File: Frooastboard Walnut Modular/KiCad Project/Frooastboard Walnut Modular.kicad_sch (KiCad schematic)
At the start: 68 parts, among them J1 SW Interface, J2 Conn_02x10_Odd_Even, U1 RP2040, U2 SPX3819M5-L-3-3, U3 W25Q32JVZP, U4 nRF8001, U5 TP4056, U6 FS312F-G, U7 FS8205, Y1 32.768kHz, Y2 16MHz, Y3 12MHz

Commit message: Switch to IP2312
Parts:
- removed C28: 10u, Capacitor_SMD:C_0805_2012Metric, symbol Device:C_Small
- removed R11: 1k2, Resistor_SMD:R_0805_2012Metric, symbol Device:R_Small
- removed U5: TP4056, Package_SO:SOIC-8-1EP_3.9x4.9mm_P1.27mm_EP2.41x3.3mm, symbol Frooastboard Symbols:TP4056
- added C?: 22u, symbol Device:C
- added C? (x2): 10u, symbol Device:C
- added L?: 1uH, symbol Device:L
- added R? (x2): 0k1, symbol Device:R
- added R?: 2R, symbol Device:R
- added R?: 1k, Resistor_SMD:R_0805_2012Metric, symbol Device:R_Small
- added R?: 51k, symbol Device:R
- added U?: IP2312, Package_SO:SOIC-8-1EP_3.9x4.9mm_P1.27mm_EP2.41x3.3mm, symbol Frooastboard Symbols:IP2312
- C30: value 100n -> 22u
- R12: value 100R -> 0k5
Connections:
- net BATT+ is gone; now on net BATTERY+: R12.1, R13.1, TP6.2, U2.1 (IN), U2.3 (EN)
- net +5V: now also C?.1, C?.1, R?.1, U?.8 (VIN)
- net GND: now also C?.2, C?.2, C?.2, R?.1, U?.9 (EP)
- net BATTERY+: now reaches C30.1, U6.5 (VCC)
- net BATTERY+: now also L?.2, R?.1; no longer R12.2
- net BATT-: now reaches C30.2, TP6.1, U6.6 (GND), U7.3 (S2)
- new net: R?.2, U?.1 (D1)
- new net: R12.2, U?.5 (BAT)
- new net: C?.1, R?.2
- new net: R?.2, U?.2 (TEST)
- new net: R?.2, U?.3 (D2)
- new net: L?.1, U?.7 (SW)
- new net: R?.2, U?.4 (NTC)
- new net LED_CHARGING: R?.1
- new net LED_FULL: R?.1
- no-connect marks 5 -> 9
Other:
- note added: "NC for 2.1A"
- note added: "NC for 4.2V"
- moved on the sheet: C14, C15, C16, C17, C18, C19, C20, C21, C22, C23, C24, C25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

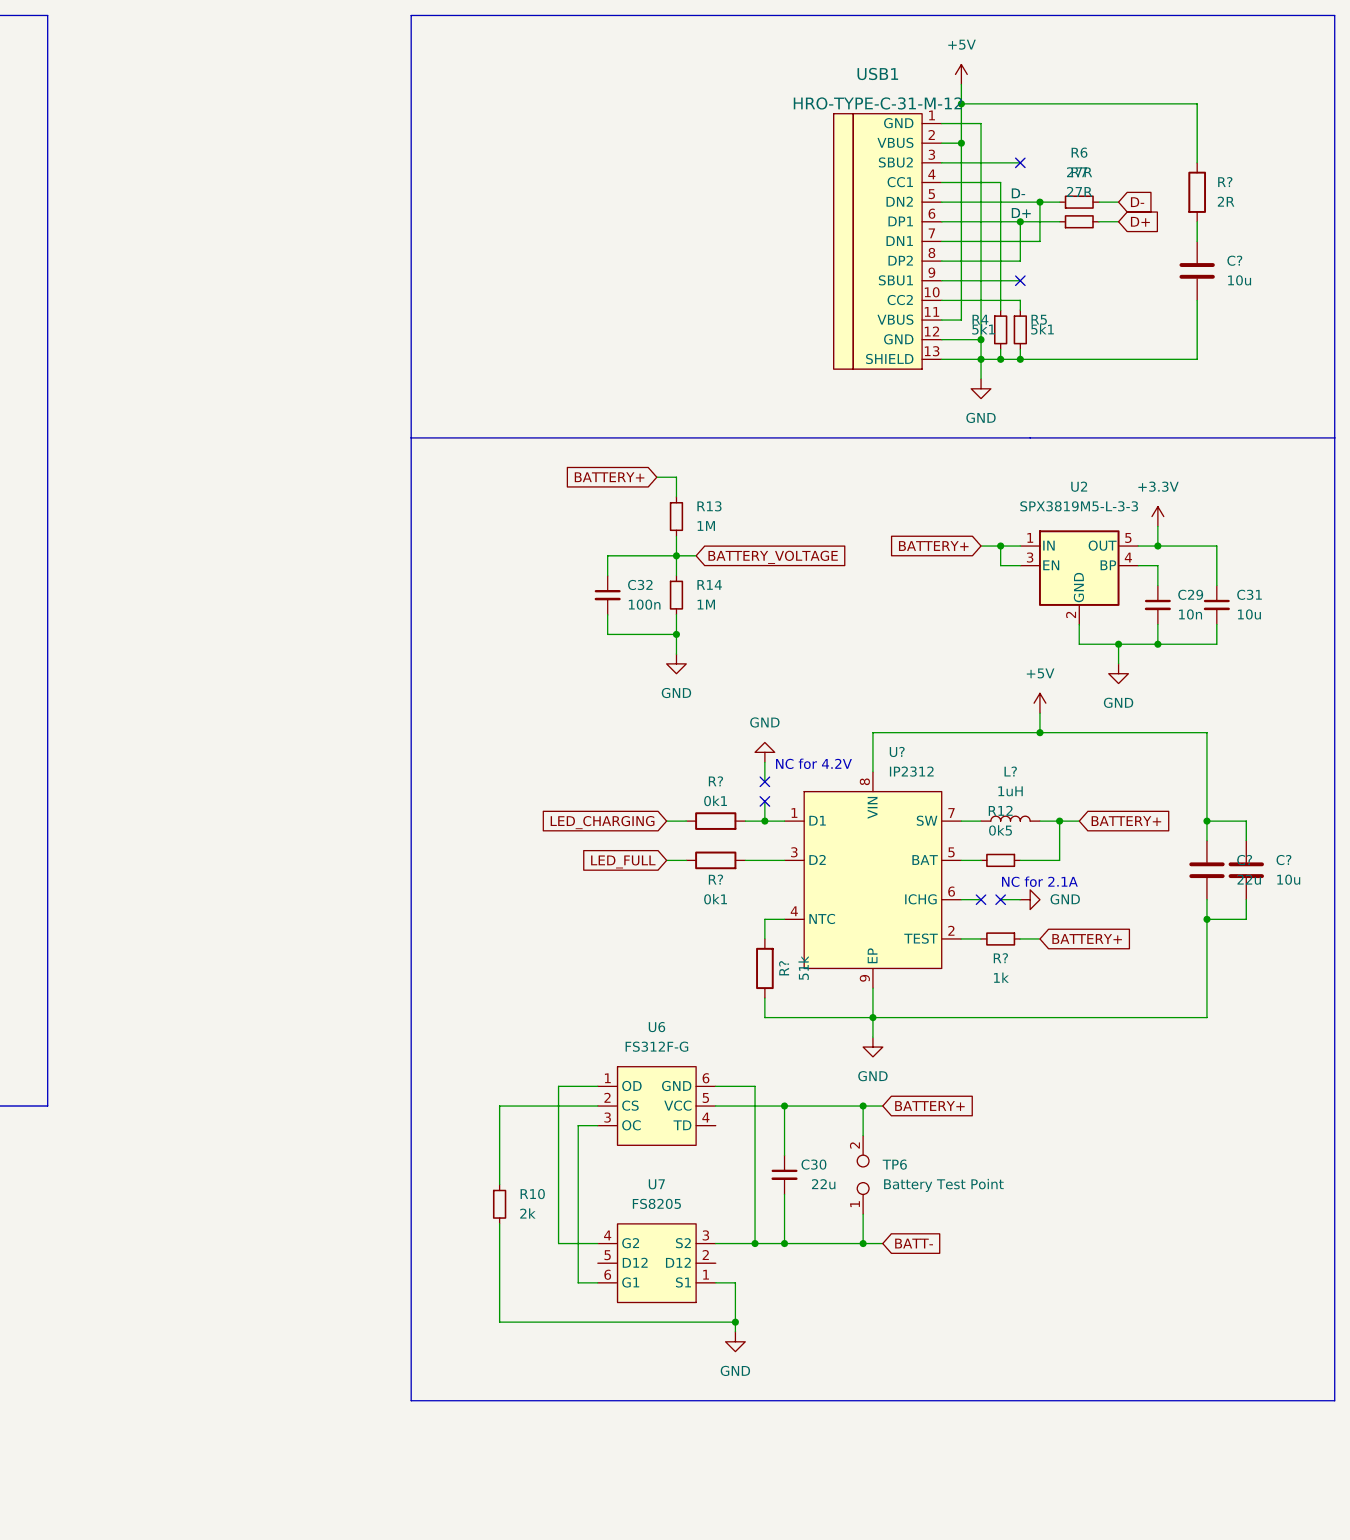
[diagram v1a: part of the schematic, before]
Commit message: Update Frooastboard Walnut Modular.kicad_sch
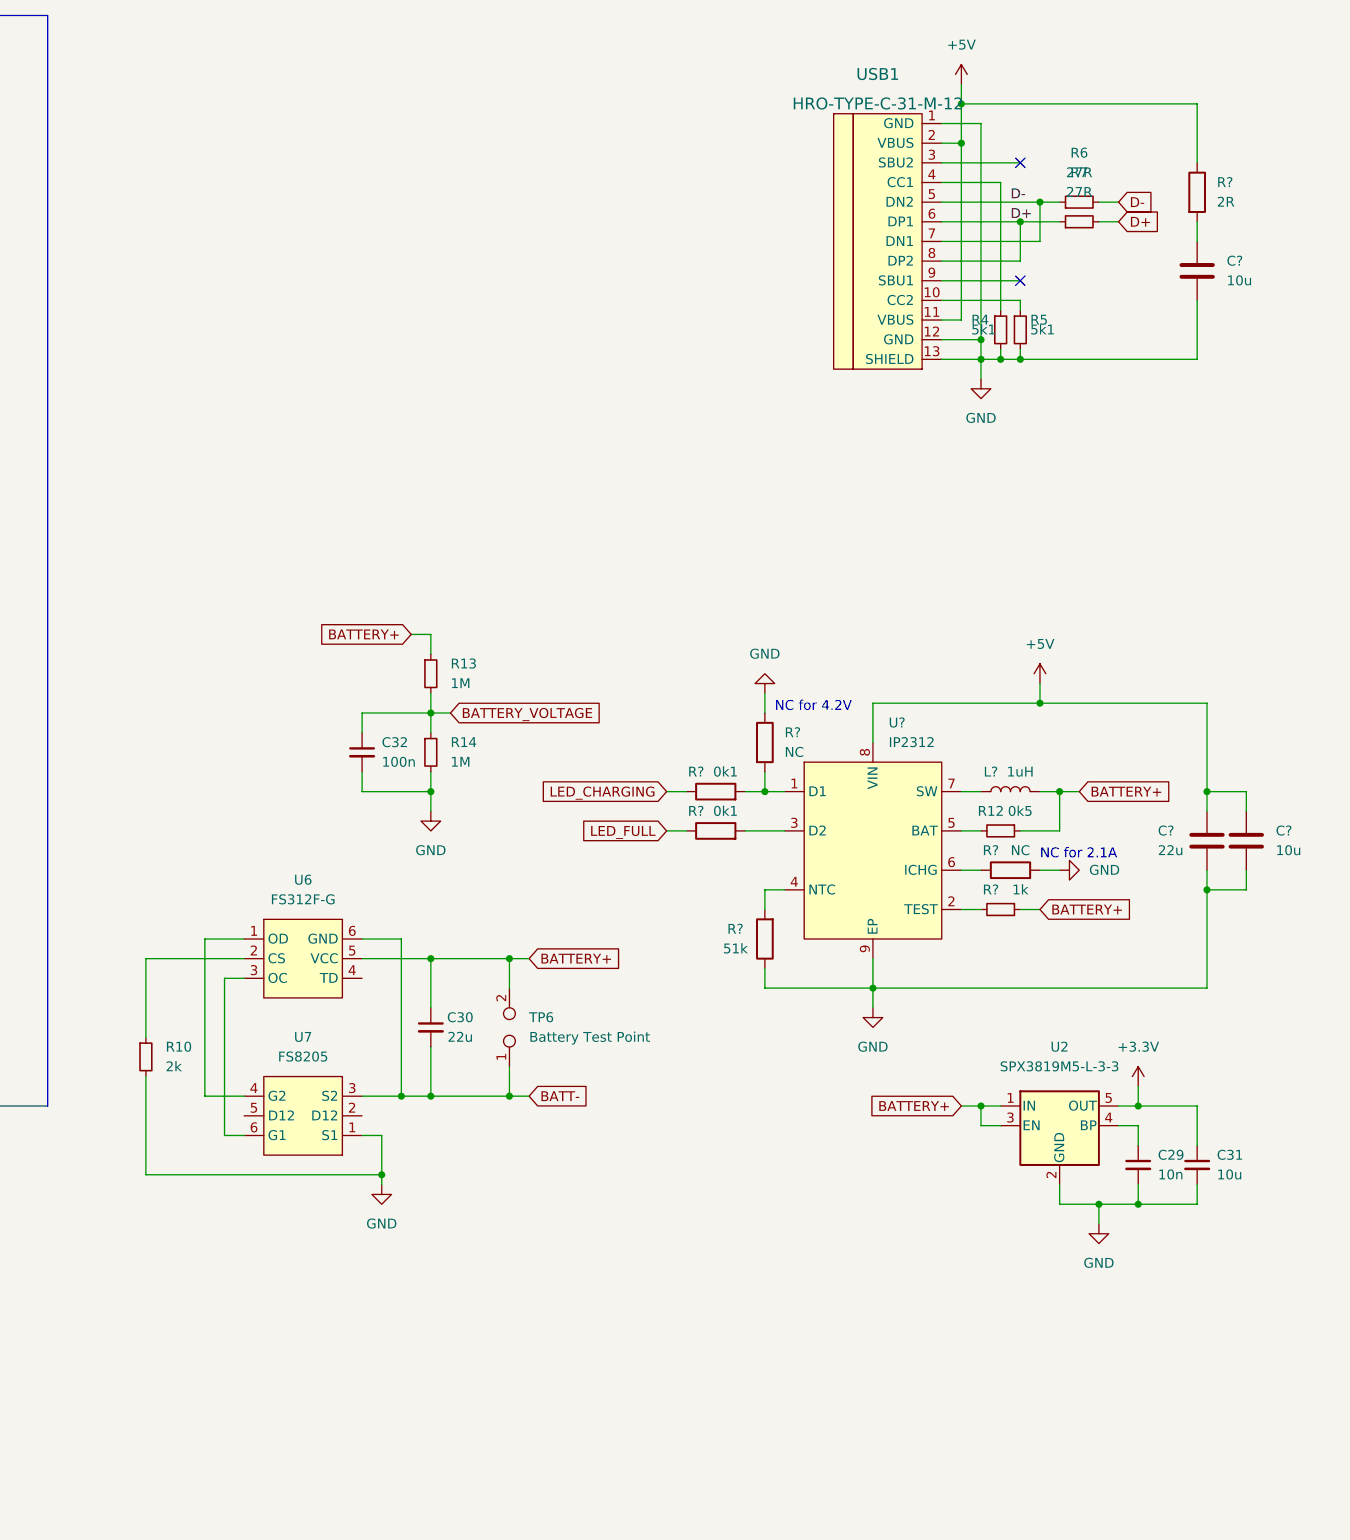
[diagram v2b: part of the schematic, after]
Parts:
- added R? (x2): NC, symbol Device:R
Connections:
- net GND: now also R?.1, R?.2
- net at R?.2, U?.1 (D1): now also R?.2
- net at U?.6 (ICHG): now also R?.1
- no-connect marks 9 -> 5
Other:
- moved on the sheet: C29, C30, C31, C32, C?, L?, R10, R12, R13, R14, R?, TP6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

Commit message: do some stuff
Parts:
- removed C?: 10u, symbol Device:C
- removed J2: Conn_02x10_Odd_Even, symbol Connector_Generic:Conn_02x10_Odd_Even
- removed R4, R5: 5k1, Resistor_SMD:R_0805_2012Metric, symbol Device:R_Small
- removed R6, R7: 27R, Resistor_SMD:R_0805_2012Metric, symbol Device:R_Small
- removed R?: 2R, symbol Device:R
- removed USB1: HRO-TYPE-C-31-M-12, Type_C:HRO-TYPE-C-31-M-12, symbol Type-C:HRO-TYPE-C-31-M-12
- added C28: 0.1u, Capacitor_SMD:C_0805_2012Metric, symbol Device:C_Small
- added C33: 10u, Capacitor_SMD:C_0805_2012Metric, symbol Device:C_Small
- added C34, C35: 10u, Capacitor_Tantalum_SMD:CP_EIA-2012-15_AVX-P, symbol Device:C_Polarized
- added D1: GREEN, symbol Device:LED
- added D10, D100, D101, D102, D103, D104, D11, D12, D13, D14, D17, D18, D19, D20, D24, D25, D26, D27, D3, D30, D31, D32, D33, D37, D38, D39, D4, D40, D43, D44, D45, D46, D49, D5, D50, D51, D52, D55, D56, D57, D58, D59, D6, D60, D61, D62, D7, D74, D75, D76, D77, D8, D89, D9, D90, D91, D92, D93, D94, D95, D96, D97, D98, D99: RGB_LED_6_Pin, Frooastboard Footprints:Everlight 99-235, symbol Frooastboard Symbols:RGB_LED_6_Pin
- added D15, D16, D21, D22, D23, D28, D29, D34, D35, D36, D41, D42, D47, D48, D53, D54, D63, D64, D65, D66, D67, D68, D69, D70, D71, D72, D73, D78, D79, D80, D81, D82, D83, D84, D85, D86, D87, D88: D_Small, symbol Device:D_Small
- added D2: RED, symbol Device:LED
- added J10: Conn_01x13_Male, symbol Connector:Conn_01x13_Male
- added J11: Conn_01x13_Female, symbol Connector:Conn_01x13_Female
- added J2: Conn_01x16, symbol Connector_Generic:Conn_01x16
- added J3, J4: Conn_01x06, symbol Connector_Generic:Conn_01x06
- added J5: Conn_01x10, symbol Connector_Generic:Conn_01x10
- added J6: Conn_01x12, symbol Connector_Generic:Conn_01x12
- added J7: Conn_01x04, symbol Connector_Generic:Conn_01x04
- added J8: Conn_01x10_Male, symbol Connector:Conn_01x10_Male
- added J9: Conn_01x10_Female, symbol Connector:Conn_01x10_Female
- added M1: Frooastboard_MM2040, symbol Frooastboard Symbols:Frooastboard_MM2040
- added MX1, MX10, MX11, MX12, MX13, MX14, MX15, MX16, MX17, MX18, MX19, MX2, MX20, MX21, MX22, MX23, MX24, MX25, MX26, MX27, MX28, MX29, MX3, MX30, MX31, MX32, MX33, MX34, MX35, MX36, MX37, MX38, MX4, MX5, MX6, MX7, MX8, MX9: MX-NoLED, symbol MX_Alps_Hybrid:MX-NoLED
- added R11, R7: 100k, Resistor_SMD:R_0805_2012Metric, symbol Device:R
- added R4, R5: 2k, Resistor_SMD:R_0805_2012Metric, symbol Device:R
- added R6: 20k, Resistor_SMD:R_0805_2012Metric, symbol Device:R
- added U5: IS31FL3733-QF, Package_DFN_QFN:QFN-48-1EP_6x6mm_P0.4mm_EP4.2x4.2mm, symbol Driver_LED:IS31FL3733-QF
- U1: footprint Frooastboard Footprints:RP2040-QFN-56 -> Sleep-Lib:RP2040-QFN-56
- gave numbers to parts that had none: 10
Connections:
- net +3V3: now also C28.2, C33.1, C34.1, C35.1, R11.2, R4.1, R5.1, U5.20 (PVCC), U5.29 (PVCC), U5.37 (AVCC), U5.38 (DVCC), U5.39 (VIO)
- net +5V: now also J7.1 (Pin_1)
- net COL0: now also J5.1 (Pin_1), J9.1 (Pin_1)
- net COL1: now also J5.2 (Pin_2), J9.2 (Pin_2)
- net COL2: now also J5.3 (Pin_3), J9.3 (Pin_3)
- net COL3: now also J5.4 (Pin_4), J9.4 (Pin_4)
- net COL4: now also J5.5 (Pin_5), J9.5 (Pin_5)
- net COL5: now also J5.6 (Pin_6), J9.6 (Pin_6)
- net COL6: now also J5.7 (Pin_7), J9.7 (Pin_7)
- net COL7: now also J5.8 (Pin_8), J9.8 (Pin_8)
- net COL8: now also J11.1 (Pin_1), J5.9 (Pin_9)
- net COL9: now also J11.2 (Pin_2), J5.10 (Pin_10)
- net GND: now also C28.1, C33.2, C34.2, C35.2, D1.1 (K), D2.1 (K), J7.2 (Pin_2), R6.2, R7.2, U5.12 (PGND), U5.34 (AGND), U5.43 (ADDR1), U5.44 (ADDR2), U5.48 (GND), U5.49 (GND), U5.5 (PGND)
- net LED_CHARGING: now also D2.2 (A)
- net LED_FULL: now also D1.2 (A)
- net ROW0: now also J11.3 (Pin_3), J6.1 (Pin_1)
- net ROW1: now also J11.4 (Pin_4), J6.2 (Pin_2)
- net ROW2: now also J11.5 (Pin_5), J6.3 (Pin_3)
- net ROW3: now also J11.6 (Pin_6), J6.4 (Pin_4)
- net ROW4: now also J11.7 (Pin_7), J6.5 (Pin_5)
- net ROW5: now also J11.8 (Pin_8), J6.6 (Pin_6)
- net ROW6: now also J11.9 (Pin_9), J6.7 (Pin_7)
- net ROW7: now also J11.10 (Pin_10), J6.8 (Pin_8)
- net ROW8: now also J11.11 (Pin_11), J6.9 (Pin_9)
- net ROW9: now also J11.12 (Pin_12), J6.10 (Pin_10), J9.9 (Pin_9)
- net SCL: now also R5.2, U5.42 (SCL)
- net SDA: now also R4.2, U5.41 (SDA)
- net ROW10: now reaches U1.37 (GPIO25)
- net ROW10: now also J11.13 (Pin_13), J6.11 (Pin_11), J9.10 (Pin_10)
- net D+ renamed RP_D+
- net RP_D+: now also J7.3 (Pin_3)
- net D- renamed RP_D-
- net RP_D-: now also J7.4 (Pin_4)
- new net: J8.3 (Pin_3), MX5.1 (COL), MX6.1 (COL)
- new net: D23.2 (A), MX5.2 (ROW)
- new net: D16.1 (K), D22.1 (K), D28.1 (K), D34.1 (K), D36.1 (K), D42.1 (K), D48.1 (K), D54.1 (K), J8.10 (Pin_10)
- new net: D48.2 (A), MX14.2 (ROW)
- new net: J8.1 (Pin_1), MX1.1 (COL), MX2.1 (COL)
- new net: J8.2 (Pin_2), MX3.1 (COL), MX4.1 (COL)
- new net: J8.4 (Pin_4), MX7.1 (COL), MX8.1 (COL)
- new net: J8.5 (Pin_5), MX10.1 (COL), MX9.1 (COL)
- new net: J8.6 (Pin_6), MX11.1 (COL), MX12.1 (COL)
- new net: J8.7 (Pin_7), MX13.1 (COL), MX14.1 (COL)
- new net: J8.8 (Pin_8), MX15.1 (COL), MX16.1 (COL)
- new net: D15.1 (K), D21.1 (K), D23.1 (K), D29.1 (K), D35.1 (K), D41.1 (K), D47.1 (K), D53.1 (K), J8.9 (Pin_9)
- new net: J10.1 (Pin_1), MX17.1 (COL), MX18.1 (COL), MX19.1 (COL), MX20.1 (COL), MX21.1 (COL), MX22.1 (COL), MX23.1 (COL), MX24.1 (COL), MX25.1 (COL), MX26.1 (COL), MX27.1 (COL)
- new net: D71.2 (A), MX25.2 (ROW)
- new net: D36.2 (A), MX10.2 (ROW)
- new net: D73.1 (K), D88.1 (K), J10.12 (Pin_12)
- new net: D73.2 (A), MX27.2 (ROW)
- new net: D16.2 (A), MX2.2 (ROW)
- new net: D47.2 (A), MX13.2 (ROW)
- new net: D88.2 (A), MX38.2 (ROW)
- new net: J10.2 (Pin_2), MX28.1 (COL), MX29.1 (COL), MX30.1 (COL), MX31.1 (COL), MX32.1 (COL), MX33.1 (COL), MX34.1 (COL), MX35.1 (COL), MX36.1 (COL), MX37.1 (COL), MX38.1 (COL)
- new net: D82.2 (A), MX32.2 (ROW)
- new net: D41.2 (A), MX11.2 (ROW)
- new net: D80.2 (A), MX30.2 (ROW)
- new net: D64.2 (A), MX18.2 (ROW)
- new net: D70.2 (A), MX24.2 (ROW)
- new net: D15.2 (A), MX1.2 (ROW)
- new net: D66.2 (A), MX20.2 (ROW)
- new net: D63.1 (K), D78.1 (K), J10.3 (Pin_3)
- new net: D78.2 (A), MX28.2 (ROW)
- new net: D22.2 (A), MX4.2 (ROW)
- new net: D72.1 (K), D87.1 (K), J10.10 (Pin_10)
- new net: D67.1 (K), D82.1 (K), J10.11 (Pin_11)
- new net: D68.1 (K), D83.1 (K), J10.13 (Pin_13)
- new net: D69.1 (K), D84.1 (K), J10.4 (Pin_4)
- new net: D64.1 (K), D79.1 (K), J10.5 (Pin_5)
- new net: D70.1 (K), D85.1 (K), J10.6 (Pin_6)
- new net: D65.1 (K), D80.1 (K), J10.7 (Pin_7)
- new net: D71.1 (K), D86.1 (K), J10.8 (Pin_8)
- new net: D66.1 (K), D81.1 (K), J10.9 (Pin_9)
- new net: D21.2 (A), MX3.2 (ROW)
- new net: D81.2 (A), MX31.2 (ROW)
- new net: D42.2 (A), MX12.2 (ROW)
- new net: D83.2 (A), MX33.2 (ROW)
- new net: D29.2 (A), MX7.2 (ROW)
- new net: D84.2 (A), MX34.2 (ROW)
- new net: D35.2 (A), MX9.2 (ROW)
- new net: D86.2 (A), MX36.2 (ROW)
- new net: D67.2 (A), MX21.2 (ROW)
- new net: D69.2 (A), MX23.2 (ROW)
- new net: D53.2 (A), MX15.2 (ROW)
- new net: D28.2 (A), MX6.2 (ROW)
- new net: D79.2 (A), MX29.2 (ROW)
- new net: D85.2 (A), MX35.2 (ROW)
- new net: D68.2 (A), MX22.2 (ROW)
- new net: D87.2 (A), MX37.2 (ROW)
- new net: D72.2 (A), MX26.2 (ROW)
- new net: D54.2 (A), MX16.2 (ROW)
- new net: D65.2 (A), MX19.2 (ROW)
- new net: D34.2 (A), MX8.2 (ROW)
- new net: D63.2 (A), MX17.2 (ROW)
- new net CS1: J2.1 (Pin_1), U5.16 (CS1)
- new net CS10: J2.10 (Pin_10), U5.26 (CS10)
- new net CS11: J2.11 (Pin_11), U5.27 (CS11)
- new net CS12: J2.12 (Pin_12), U5.28 (CS12)
- new net CS13: J2.13 (Pin_13), U5.30 (CS13)
- new net CS14: J2.14 (Pin_14), U5.31 (CS14)
- new net CS15: J2.15 (Pin_15), U5.32 (CS15)
- new net CS16: J2.16 (Pin_16), U5.33 (CS16)
- new net CS2: J2.2 (Pin_2), U5.17 (CS2)
- new net CS3: J2.3 (Pin_3), U5.18 (CS3)
- new net CS4: J2.4 (Pin_4), U5.19 (CS4)
- new net CS5: J2.5 (Pin_5), U5.21 (CS5)
- new net CS6: J2.6 (Pin_6), U5.22 (CS6)
- new net CS7: J2.7 (Pin_7), U5.23 (CS7)
- new net CS8: J2.8 (Pin_8), U5.24 (CS8)
- new net CS9: J2.9 (Pin_9), U5.25 (CS9)
- new net IICRST: R7.1, U5.47 (IICRST)
- new net RSET: R6.1, U5.35 (RSET)
- new net SDB: R11.1, U5.46 (~{SDB})
- new net SW1: J3.1 (Pin_1), U5.2 (SW1)
- new net SW10: J4.4 (Pin_4), U5.13 (SW10)
- new net SW11: J4.5 (Pin_5), U5.14 (SW11)
- new net SW12: J4.6 (Pin_6), U5.15 (SW12)
- new net SW2: J3.2 (Pin_2), U5.3 (SW2)
- new net SW3: J3.3 (Pin_3), U5.4 (SW3)
- new net SW4: J3.4 (Pin_4), U5.6 (SW4)
- new net SW5: J3.5 (Pin_5), U5.7 (SW5)
- new net SW6: J3.6 (Pin_6), U5.8 (SW6)
- new net SW7: J4.1 (Pin_1), U5.9 (SW7)
- new net SW8: J4.2 (Pin_2), U5.10 (SW8)
- new net SW9: J4.3 (Pin_3), U5.11 (SW9)
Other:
- added sheet Main (Main.kicad_sch)
- moved on the sheet: C1, C10, C11, C12, C13, C2, C29, C3, C30, C31, C32, C36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

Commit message: almost finish schematic
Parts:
- removed D10, D100, D101, D102, D103, D104, D11, D12, D13, D14, D17, D18, D19, D20, D24, D25, D26, D27, D3, D30, D31, D32, D33, D37, D38, D39, D4, D40, D43, D44, D45, D46, D49, D5, D50, D51, D52, D55, D56, D57, D58, D59, D6, D60, D61, D62, D7, D74, D75, D76, D77, D8, D89, D9, D90, D91, D92, D93, D94, D95, D96, D97, D98, D99: RGB_LED_6_Pin, Frooastboard Footprints:Everlight 99-235, symbol Frooastboard Symbols:RGB_LED_6_Pin
- removed D15, D16, D21, D22, D23, D28, D29, D34, D35, D36, D41, D42, D47, D48, D53, D54, D63, D64, D65, D66, D67, D68, D69, D70, D71, D72, D73, D78, D79, D80, D81, D82, D83, D84, D85, D86, D87, D88: D_Small, symbol Device:D_Small
- removed J10: Conn_01x13_Male, symbol Connector:Conn_01x13_Male
- removed J11: Conn_01x13_Female, symbol Connector:Conn_01x13_Female
- removed J8: Conn_01x10_Male, symbol Connector:Conn_01x10_Male
- removed J9: Conn_01x10_Female, symbol Connector:Conn_01x10_Female
- removed M1: Frooastboard_MM2040, symbol Frooastboard Symbols:Frooastboard_MM2040
- removed MX1, MX10, MX11, MX12, MX13, MX14, MX15, MX16, MX17, MX18, MX19, MX2, MX20, MX21, MX22, MX23, MX24, MX25, MX26, MX27, MX28, MX29, MX3, MX30, MX31, MX32, MX33, MX34, MX35, MX36, MX37, MX38, MX4, MX5, MX6, MX7, MX8, MX9: MX-NoLED, symbol MX_Alps_Hybrid:MX-NoLED
- added R23, R24: 27R, Resistor_SMD:R_0805_2012Metric, symbol Device:R_Small
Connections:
- net RP_D+: now also R23.1; no longer J7.3 (Pin_3)
- net RP_D-: now also R24.1; no longer J7.4 (Pin_4)
- new net: J7.3 (Pin_3), R23.2
- new net: J7.4 (Pin_4), R24.2
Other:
- added sheet F Row (F Row.kicad_sch)
- added sheet Numpad (Numpad.kicad_sch)
- moved on the sheet: C1, C10, C11, C12, C13, C17, C19, C2, C21, C22, C23, C24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

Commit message: before nrf52810
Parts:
- removed C30: 22u, Capacitor_SMD:C_0805_2012Metric, symbol Device:C_Small
- removed R10: 2k, Resistor_SMD:R_0805_2012Metric, symbol Device:R_Small
- removed R12: 0k5, Resistor_SMD:R_0805_2012Metric, symbol Device:R_Small
- removed R19: 1k, Resistor_SMD:R_0805_2012Metric, symbol Device:R_Small
- removed R4, R5: 2k, Resistor_SMD:R_0805_2012Metric, symbol Device:R
- removed TP6: Battery Test Point, symbol Connector:TestPoint_2Pole
- added BT1: Battery_Cell, symbol Device:Battery_Cell
- added C30: 22u, symbol Device:C
- added R10: 2k, symbol Device:R
- added R12: 0k5, symbol Device:R
- added R19: 1k, symbol Device:R
- added R4, R5: 2k, symbol Device:R_Small
- added U?: nRF52810-QCxx, Package_DFN_QFN:QFN-32-1EP_5x5mm_P0.5mm_EP3.6x3.6mm, symbol MCU_Nordic:nRF52810-QCxx
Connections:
- net +3V3: now also R4.2, R5.2
- net GND: now also R10.1
- net NRF_MISO: no longer U1.31 (GPIO20)
- net NRF_MOSI: no longer U1.30 (GPIO19)
- net NRF_SCK: no longer U1.29 (GPIO18)
- net RP_RESET: no longer R8.2, U1.26 (~{RUN})
- net SCL: now also R5.1
- net SDA: now also R4.1
- net at U8.5 (BAT): now also R12.1
- net at U8.2 (TEST): now also R19.1
- net at U6.2 (CS): now also R10.2
- net BATT- renamed -BATT
- net -BATT: now also BT1.2 (-), C30.2
- net BATTERY+ renamed +BATT
- net +BATT: now also BT1.1 (+), C30.1, R12.2, R19.2
- net COL0: no longer names the net of J5.1 (Pin_1), U1.2 (GPIO0)
- net COL1: no longer names the net of J5.2 (Pin_2), U1.3 (GPIO1)
- net COL2: no longer names the net of J5.3 (Pin_3), U1.4 (GPIO2)
- net COL3: no longer names the net of J5.4 (Pin_4), U1.5 (GPIO3)
- net COL4: no longer names the net of J5.5 (Pin_5), U1.6 (GPIO4)
- net COL5: no longer names the net of J5.6 (Pin_6), U1.7 (GPIO5)
- net COL6: no longer names the net of J5.7 (Pin_7), U1.8 (GPIO6)
- net COL7: no longer names the net of J5.8 (Pin_8), U1.9 (GPIO7)
- net COL8: no longer names the net of J5.9 (Pin_9), U1.11 (GPIO8)
- net COL9: no longer names the net of J5.10 (Pin_10), U1.12 (GPIO9)
- net CS1: no longer names the net of J2.1 (Pin_1), U5.16 (CS1)
- net CS10: no longer names the net of J2.10 (Pin_10), U5.26 (CS10)
- net CS11: no longer names the net of J2.11 (Pin_11), U5.27 (CS11)
- net CS12: no longer names the net of J2.12 (Pin_12), U5.28 (CS12)
- net CS13: no longer names the net of J2.13 (Pin_13), U5.30 (CS13)
- net CS14: no longer names the net of J2.14 (Pin_14), U5.31 (CS14)
- net CS15: no longer names the net of J2.15 (Pin_15), U5.32 (CS15)
- net CS16: no longer names the net of J2.16 (Pin_16), U5.33 (CS16)
- net CS2: no longer names the net of J2.2 (Pin_2), U5.17 (CS2)
- net CS3: no longer names the net of J2.3 (Pin_3), U5.18 (CS3)
- net CS4: no longer names the net of J2.4 (Pin_4), U5.19 (CS4)
- net CS5: no longer names the net of J2.5 (Pin_5), U5.21 (CS5)
- net CS6: no longer names the net of J2.6 (Pin_6), U5.22 (CS6)
- net CS7: no longer names the net of J2.7 (Pin_7), U5.23 (CS7)
- net CS8: no longer names the net of J2.8 (Pin_8), U5.24 (CS8)
- net CS9: no longer names the net of J2.9 (Pin_9), U5.25 (CS9)
- net ROW0: no longer names the net of J6.1 (Pin_1), U1.13 (GPIO10)
- net ROW1: no longer names the net of J6.2 (Pin_2), U1.14 (GPIO11)
- net ROW10: no longer names the net of U1.37 (GPIO25)
- net ROW10: no longer J6.11 (Pin_11)
- net ROW2: no longer names the net of J6.3 (Pin_3), U1.15 (GPIO12)
- net ROW3: no longer names the net of J6.4 (Pin_4), U1.16 (GPIO13)
- net ROW4: no longer names the net of J6.5 (Pin_5), U1.17 (GPIO14)
- net ROW5: no longer names the net of J6.6 (Pin_6), U1.18 (GPIO15)
- net ROW6: no longer names the net of U1.32 (GPIO21)
- net ROW6: no longer J6.7 (Pin_7)
- net ROW7: no longer names the net of U1.34 (GPIO22)
- net ROW7: no longer J6.8 (Pin_8)
- net ROW8: no longer names the net of U1.35 (GPIO23)
- net ROW8: no longer J6.9 (Pin_9)
- net ROW9: no longer names the net of U1.36 (GPIO24)
- net ROW9: no longer J6.10 (Pin_10)
- net SW1: no longer names the net of J3.1 (Pin_1), U5.2 (SW1)
- net SW10: no longer names the net of J4.4 (Pin_4), U5.13 (SW10)
- net SW11: no longer names the net of J4.5 (Pin_5), U5.14 (SW11)
- net SW12: no longer names the net of J4.6 (Pin_6), U5.15 (SW12)
- net SW2: no longer names the net of J3.2 (Pin_2), U5.3 (SW2)
- net SW3: no longer names the net of J3.3 (Pin_3), U5.4 (SW3)
- net SW4: no longer names the net of J3.4 (Pin_4), U5.6 (SW4)
- net SW5: no longer names the net of J3.5 (Pin_5), U5.7 (SW5)
- net SW6: no longer names the net of J3.6 (Pin_6), U5.8 (SW6)
- net SW7: no longer names the net of J4.1 (Pin_1), U5.9 (SW7)
- net SW8: no longer names the net of J4.2 (Pin_2), U5.10 (SW8)
- net SW9: no longer names the net of J4.3 (Pin_3), U5.11 (SW9)
- new net: R8.2, U1.26 (~{RUN})
- new net: U?.20 (VSS), U?.29 (VSS), U?.33 (VSS)
- new net: U?.25 (VDD), U?.32 (VDD), U?.9 (VDD)
- no-connect marks 5 -> 6
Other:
- moved on the sheet: C14, C15, C16, C17, C18, C19, C20, C21, C22, C23, C24, C26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
